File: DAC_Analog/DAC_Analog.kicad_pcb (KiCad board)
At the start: 2 copper layers, 100 x 100 mm, 165 parts, among them J1 SPDIF_RX_1, J10 Fix, J11 Fix, J12 Fix, J13 Fix, J14 MCLK_Test, J2 SPDIF_RX_2, J3 SPDIF_RX_3, J4 SPDIF_RX_4, J5 I2C_IN, J6 OutR, J7 OutL, J8 Alim_DAC, J9 Alim_SRC, T1 DA103C, T2 DA103C, T3 DA103C, T4 DA103C, U1 ISO154x, U10 OPA627xx, U11 TC595002ECB, U12 TPS79318, U13 SRC4392, U14 TPS79333, U15 TPS79333, U16 REG104_DCQ, U17 PCM1792A, U18 DS90LV012ATMF, U19 LMK61E2, U2 OPA627xx, U3 OPA627xx, U4 REG104_DCQ, U5 OPA627xx, U6 TC595002ECB, U7 OPA627xx, U8 OPA627xx, U9 REG104_DCQ

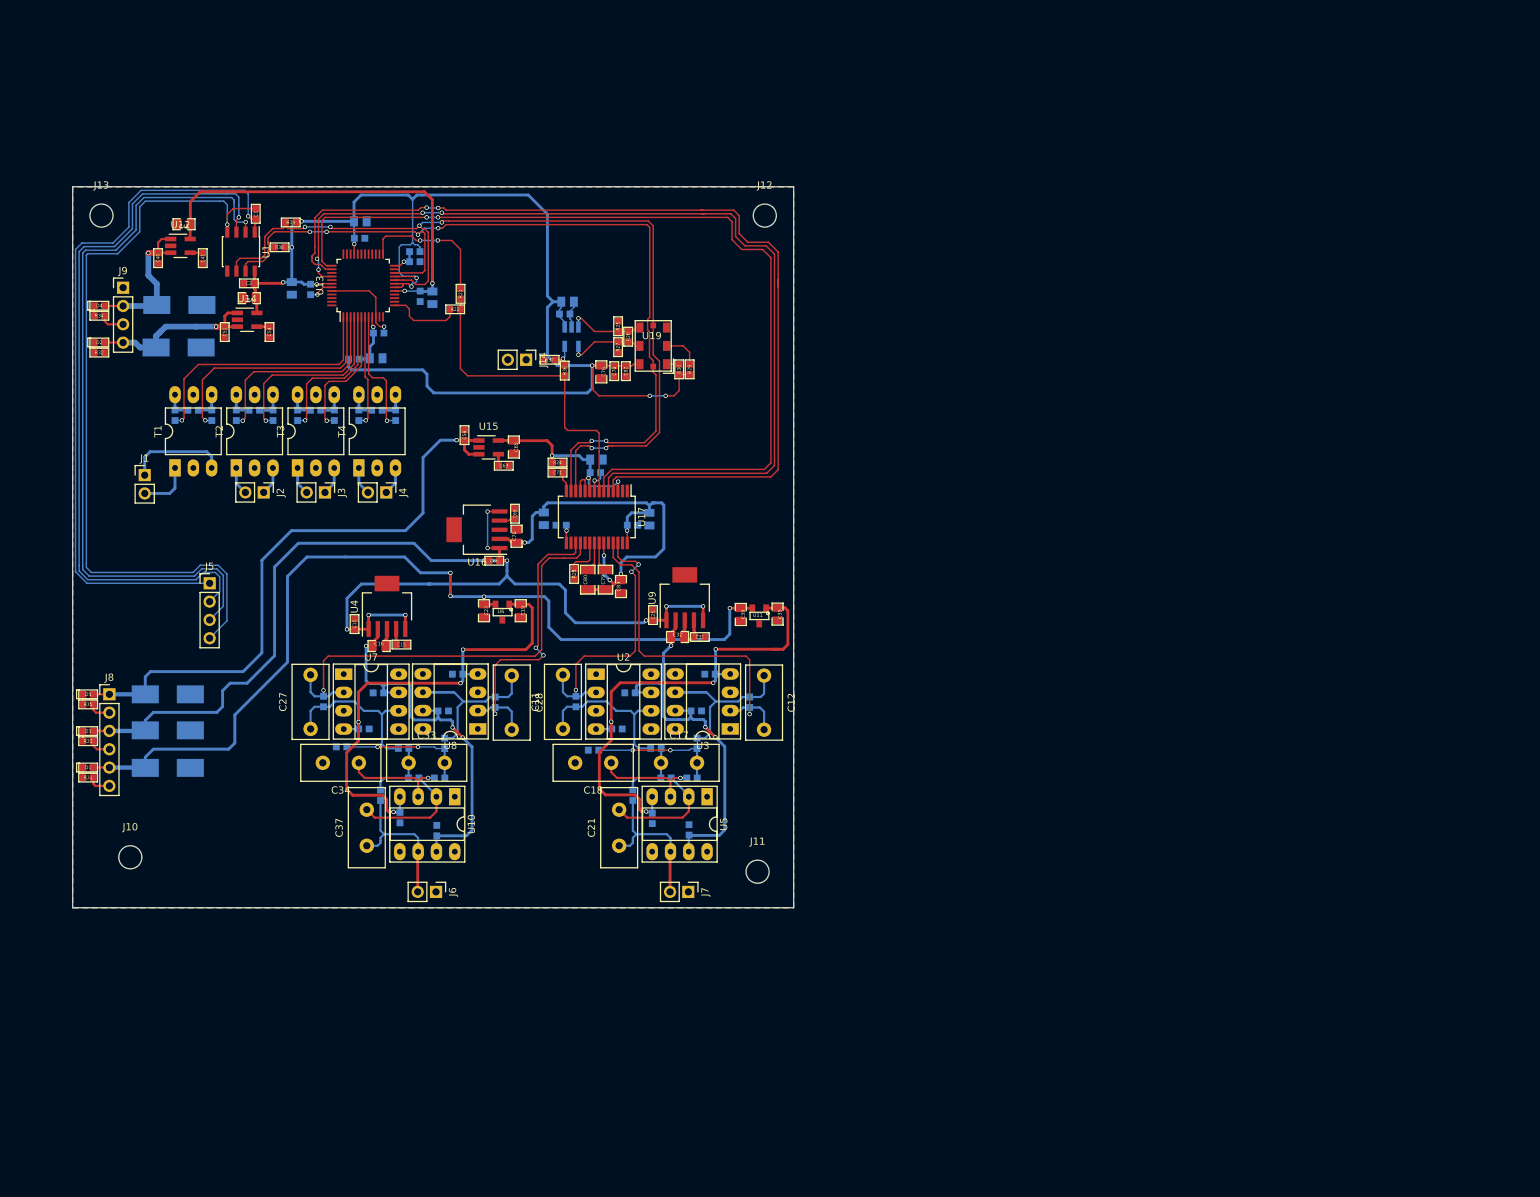
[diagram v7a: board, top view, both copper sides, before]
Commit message: Send Gerber DAC_Analog and DAC_Digital
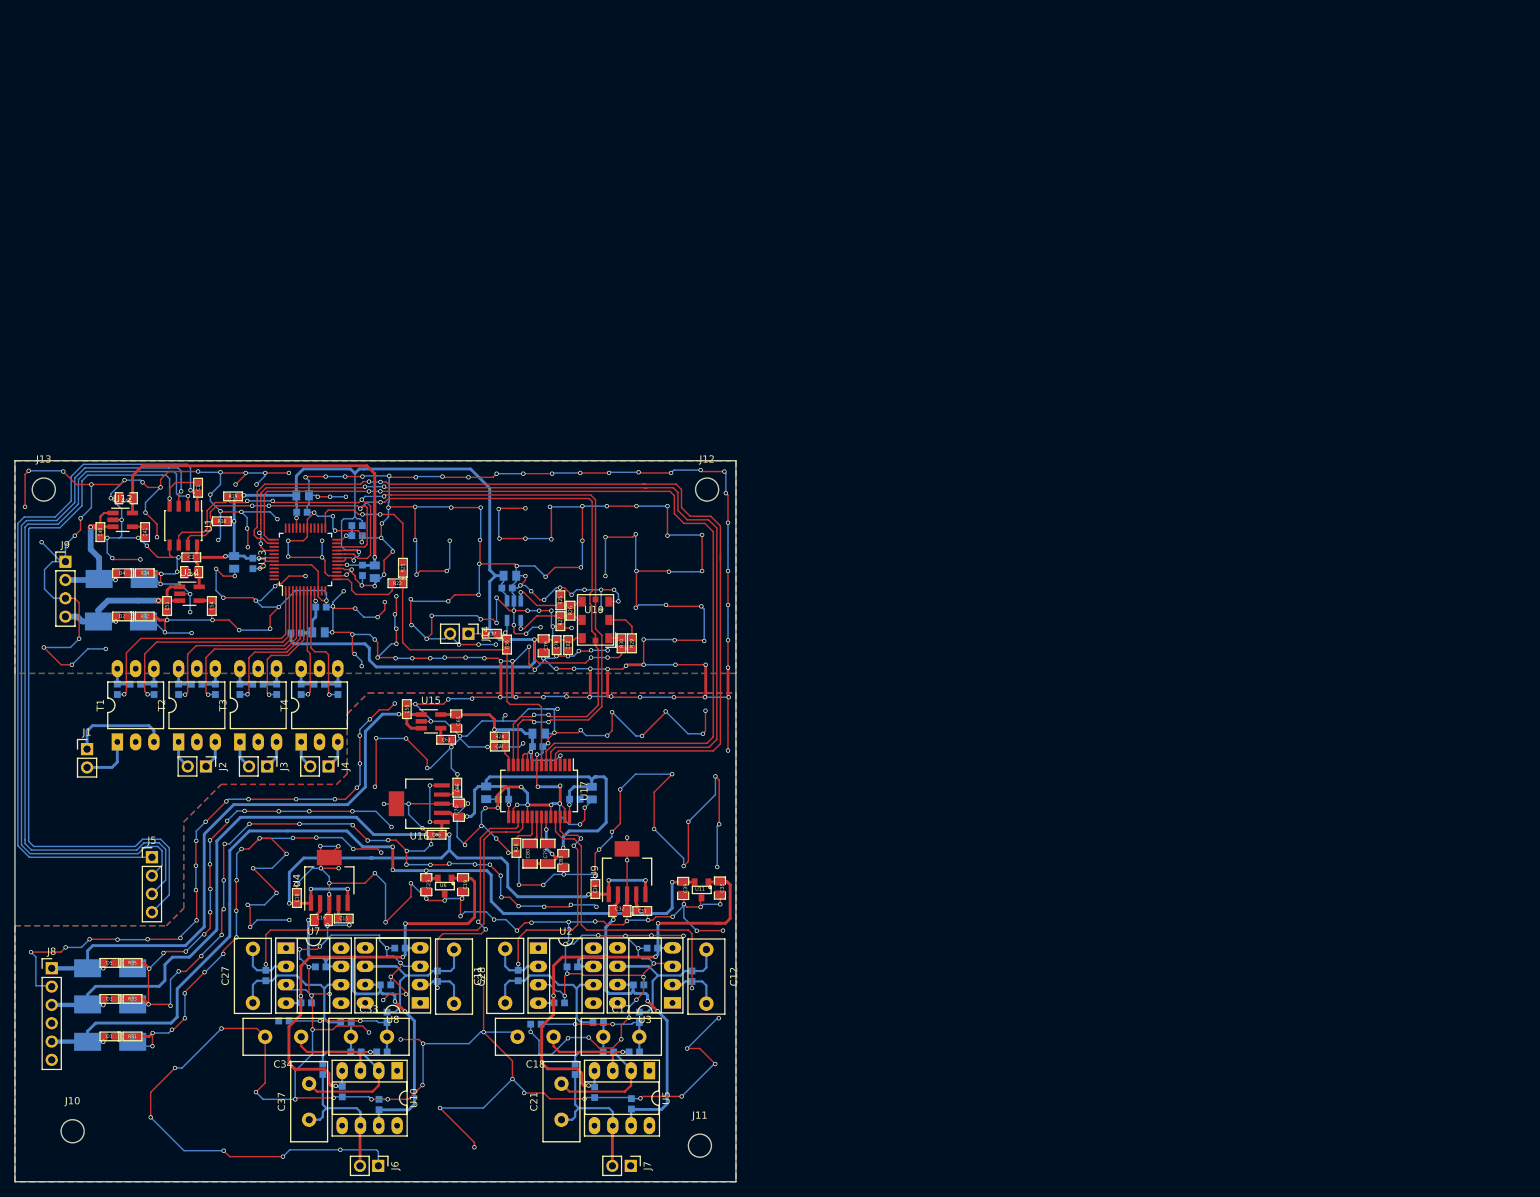
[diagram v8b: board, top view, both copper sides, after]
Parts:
- moved C12 38.8 mm to (117.9, 155.8)
- moved C19 38.8 mm to (84.2, 146.8)
- moved C23 38.8 mm to (79.0, 146.8)
- moved C28 38.8 mm to (82.9, 155.8)
- moved C74 38.8 mm to (87.3, 134.1)
- moved U17 38.8 mm to (94.7, 133.8)
- moved C2 38.8 mm to (46.5, 101.4)
- moved C40 38.8 mm to (33.9, 97.9)
- moved C41 38.8 mm to (40.0, 97.9)
- moved C60 38.8 mm to (61.8, 95.2)
- moved C61 38.8 mm to (69.5, 98.4)
- moved R38 38.8 mm to (50.7, 96.4)
- moved C1 38.8 mm to (47.4, 91.8)
- moved C10 38.8 mm to (61.1, 148.7)
- moved C15 38.8 mm to (67.6, 151.5)
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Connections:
- C4 pad 1: /-6V_anlg -> GND
- C4 pad 2: GND -> /-6V_anlg
- C40 pad 2: GNDD -> GND
- C41 pad 2: GNDD -> GND
- C42 pad 2: GNDD -> GND
- C51 pad 2: GNDD -> GND
- C52 pad 2: GNDD -> GND
- C53 pad 2: GNDD -> GND
- C54 pad 2: GNDD -> GND
- C55 pad 2: GNDD -> GND
- C56 pad 2: GNDD -> GND
- C57 pad 2: GNDD -> GND
- C58 pad 2: GNDD -> GND
- C59 pad 2: GNDD -> GND
- C60 pad 2: GNDD -> GND
- C61 pad 2: GNDD -> GND
- C62 pad 2: GNDD -> GND
- C63 pad 2: GNDD -> GND
- C64 pad 2: GNDD -> GND
- C65 pad 2: GNDD -> GND
- C66 pad 2: GNDD -> GND
- C67 pad 2: GNDD -> GND
- C68 pad 2: GNDD -> GND
- C69 pad 2: GNDD -> GND
- C70 pad 2: GNDD -> GND
- C71 pad 2: GNDD -> GND
- C72 pad 2: GNDD -> GND
- C73 pad 2: GNDD -> GND
- C74 pad 2: GNDD -> GND
- C75 pad 2: GNDD -> GND
- C76 pad 2: GNDD -> GND
- C77 pad 2: GNDD -> GND
- C78 pad 2: GNDD -> GND
- C81 pad 2: GNDD -> GND
- C82 pad 2: GNDD -> GND
- C83 pad 1: GNDD -> GND
- J14 pad 2: GNDD -> GND
- R25 pad 1: GNDD -> GND
- R27 pad 2: GNDD -> GND
- R28 pad 1: GNDD -> GND
- U12 pad 2: GNDD -> GND
- U13 pad 10: GNDD -> GND
- U13 pad 14: GNDD -> GND
- U13 pad 16: GNDD -> GND
- U13 pad 30: GNDD -> GND
- U13 pad 43: GNDD -> GND
- U13 pad 44: GNDD -> GND
- U14 pad 2: GNDD -> GND
- U15 pad 2: GNDD -> GND
- U16 pad 3: GNDD -> GND
- U16 pad 6: GNDD -> GND
- U17 pad 16: GNDD -> GND
- U17 pad 19: GNDD -> GND
- U17 pad 24: GNDD -> GND
- U17 pad 27: GNDD -> GND
- U17 pad 8: GNDD -> GND
- U18 pad 2: GNDD -> GND
- U19 pad 3: GNDD -> GND
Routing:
- net GND: track 17.7 -> 1984.2 mm, vias 0 -> 445
- net GNDD: track 22.8 -> 0.00 mm, vias 3 -> 0
- net /DigitalCv_DAC/+5V_dac: track 65.3 -> 70.0 mm
- net Net-(J14-Pad1): track 0.00 -> 2.52 mm
- net /+3.3V_rcv: track 195.9 -> 193.9 mm
- net /+6v_anlg: track 167.7 -> 168.6 mm, vias 9 -> 10
- net /+2v_dig: track 21.5 -> 22.3 mm, vias 1 -> 2
- net /-6V_anlg: track 129.0 -> 129.8 mm, vias 4 -> 5
- net /+4v_anlg: track 85.1 -> 85.9 mm, vias 1 -> 2
- net /+4v_dig: track 25.4 -> 26.0 mm, vias 1 -> 2
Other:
- board text added: "L"
- board text added: "R"
